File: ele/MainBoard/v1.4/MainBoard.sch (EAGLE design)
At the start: 130 parts, among them IC1 MCP23017SP, IC2 74HC595D, IC3 74HC595D, X1 POWER_IN, X10 M7, X2 POWER_OUT, X3 M2, X4 M4, X5 M6, X6 M8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

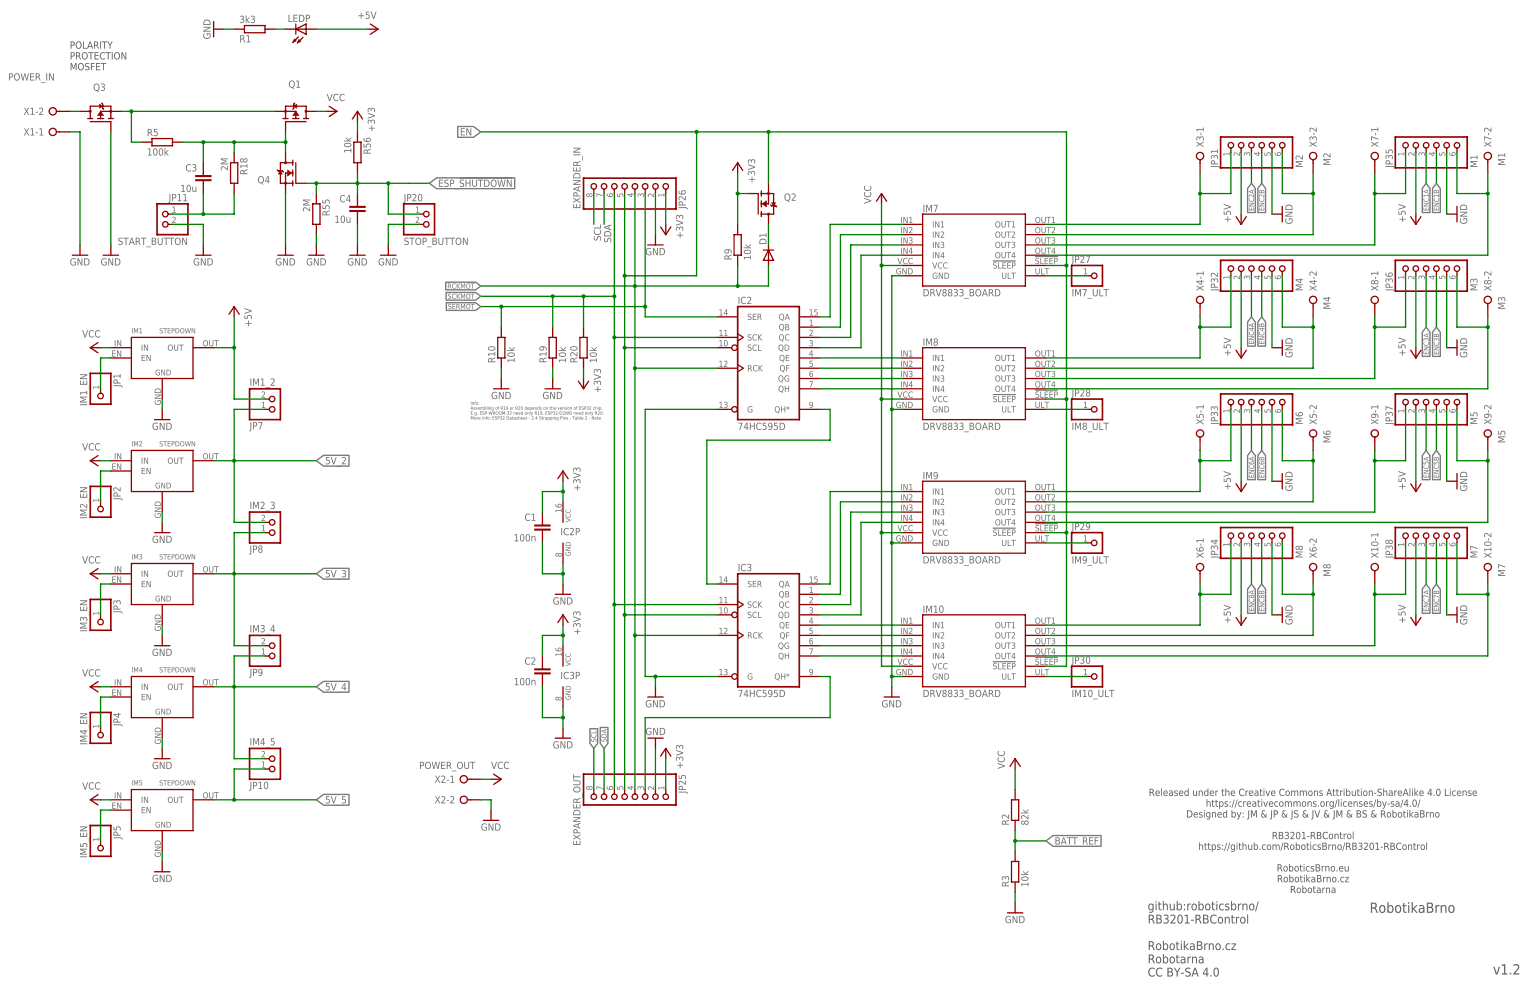
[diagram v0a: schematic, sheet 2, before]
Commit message: ele: MainBoard - Add version v1.4 and restore version v1.2 after merge
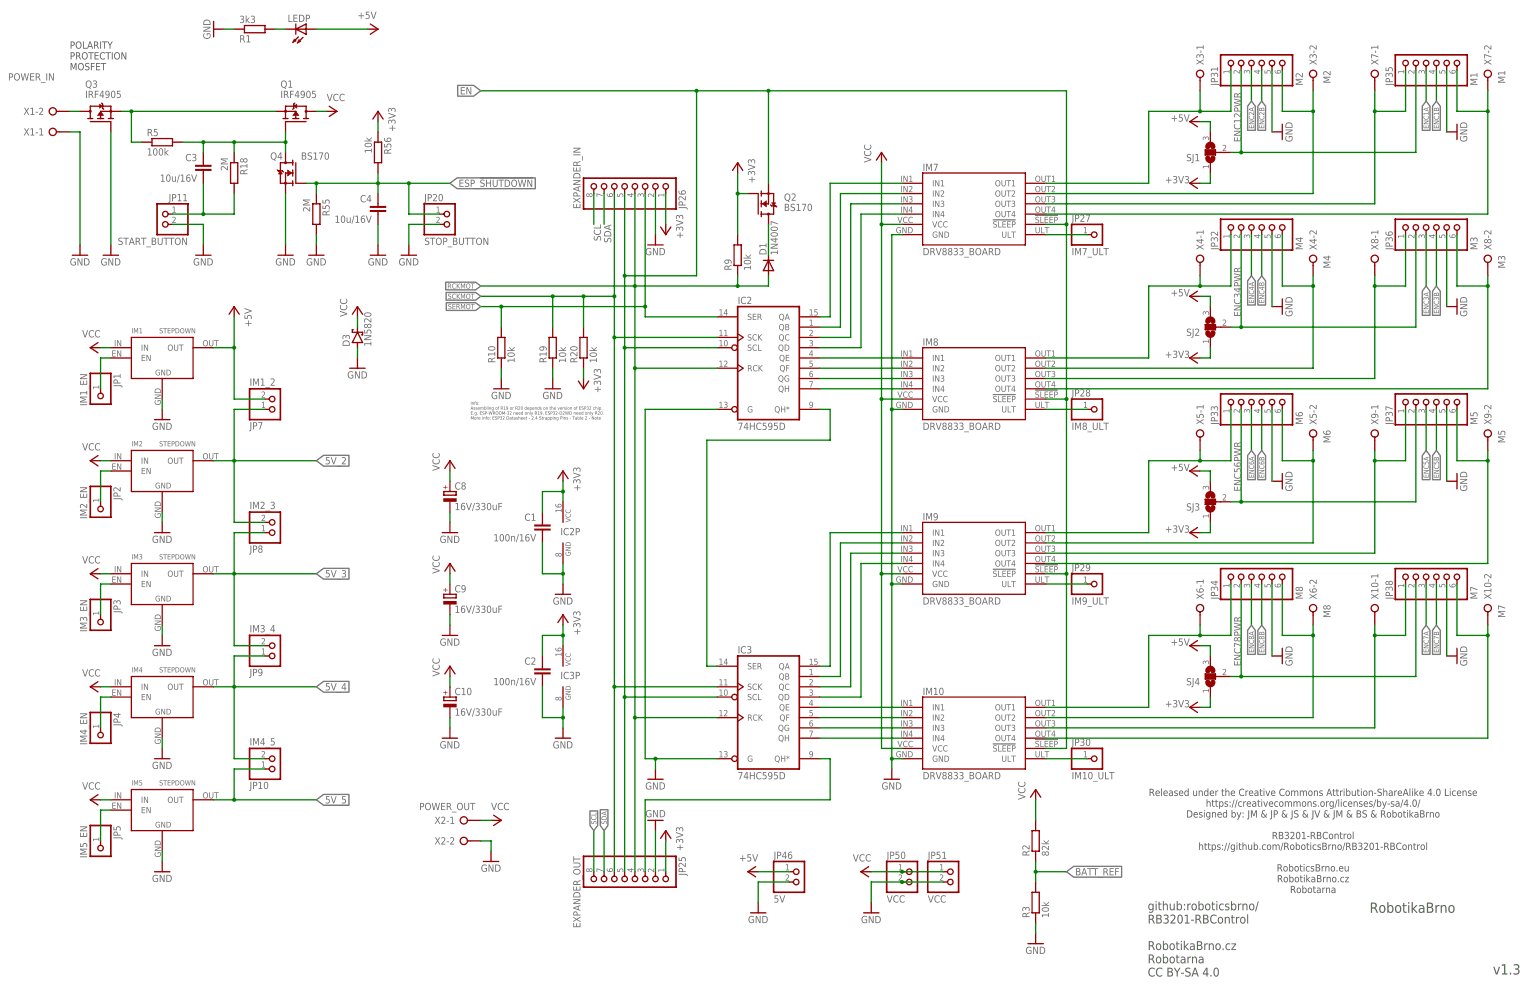
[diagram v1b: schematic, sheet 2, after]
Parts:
- added C10, C8, C9: 16V/330uF, rcl:CPOL-EUE5-10.5
- added D3: 1N5820, diode:SCHOTTKY-DIODEF126Z12
- added JP46: 5V, pinhead:PINHD-1X2
- added JP47, JP48: 292161-3, iServo_connector:292161-3
- added JP49: ISERVO, pinhead:PINHD-1X1
- added JP50, JP51: VCC, pinhead:PINHD-1X2
- added SJ1, SJ2, SJ3, SJ4: (no value), jumper:SJ2W
- added U$3: SJ_NC, SolderJumperNormallyClosed:SJ_NC
- C1, C2: value 100n -> 100n/16V
- C3, C4: value 10u -> 10u/16V
- C5, C6, C7: value 100n -> 100n/10V
- D1, D2: value (none) -> 1N4007
- JP24: device pinhead:PINHD-1X2 -> jumper:SJ
- JP42: value I2C3_3V3 -> 292161-3; device pinhead:PINHD-1X4 -> iServo_connector:292161-3
- Q1, Q3: value (none) -> IRF4905
- Q2, Q4: value (none) -> BS170
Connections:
- new net ENC12PWR: JP31.2, JP35.2, SJ1.2
- new net ENC34PWR: JP32.2, JP36.2, SJ2.2
- new net ENC56PWR: JP33.2, JP37.2, SJ3.2
- new net ENC78PWR: JP34.2, JP38.2, SJ4.2
- new net ISERVO: JP42.3, JP47.3, JP48.3, JP49.1, U$3.P$2
- net +3V3: now also SJ1.1, SJ2.1, SJ3.1, SJ4.1; no longer JP42.4
- net +5V: now also JP46.1, SJ1.3, SJ2.3, SJ3.3, SJ4.3; no longer JP31.2, JP32.2, JP33.2, JP34.2, JP35.2, JP36.2, JP37.2, JP38.2
- net ENC8A: now also U$3.P$1
- net GND: now also C10.-, C8.-, C9.-, D3.A, JP42.1, JP46.2, JP47.1, JP48.1, JP50.2, JP51.2; no longer JP42.3
- net SCL: no longer JP42.1
- net SDA: no longer JP42.2
- net VCC: now also C10.+, C8.+, C9.+, D3.C, JP42.2, JP47.2, JP48.2, JP50.1, JP51.1
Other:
- note added: "INPUT ONLY!"
- note added: "RN1-RN3 = 330R"
- note added: "RN3-RN5 = 330R"
- note added: "v1.3"
- note removed: "v1.2"
- moved on the sheet: C3, C4, D1, D2, IC3, IM10, IM7, IM9, JP20, JP25, JP27, JP29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
